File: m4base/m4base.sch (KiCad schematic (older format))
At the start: 38 parts, among them IC1 MCP2562, IC2 STM32F405RxTx, J1 WEST TOP, J2 EAST TOP, P1 SWD_TC, Y1 26M

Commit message: Create top
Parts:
- J?: value CAM -> CAN
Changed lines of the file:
@@
 encoding utf-8
 Sheet 1 1
-Title "M4_TEMPLATE"
+Title "Martlet IV Base"
 Date "2020-02-05"
 Rev "1"
 Comp "CU Spaceflight"
-Comment1 "Drawn By: Sean McGuire"
-Comment2 ""
-Comment3 ""
+Comment1 "Henry Franks"
+Comment2 "Sean McGuire"
+Comment3 "Drawn By:"
 Comment4 ""
 $EndDescr
@@
 P 6700 3250
 F 0 "J?" H 6700 3350 50  0000 C CNN
-F 1 "CAM" H 6700 3050 50  0000 C CNN
+F 1 "CAN" H 6700 3050 50  0000 C CNN
 F 2 "" H 6700 3250 50  0001 C CNN
 F 3 "" H 6700 3250 50  0001 C CNN

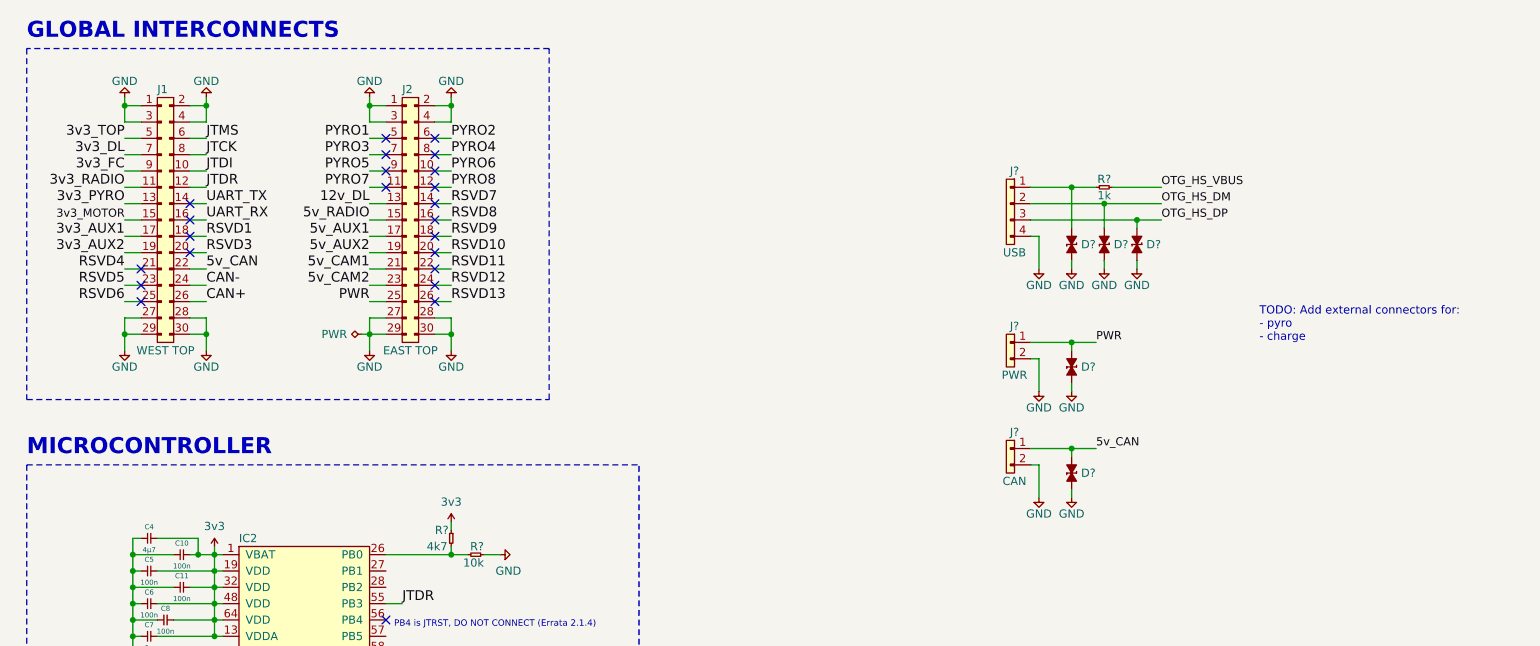
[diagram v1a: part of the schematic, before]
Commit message: Revise global interconnects
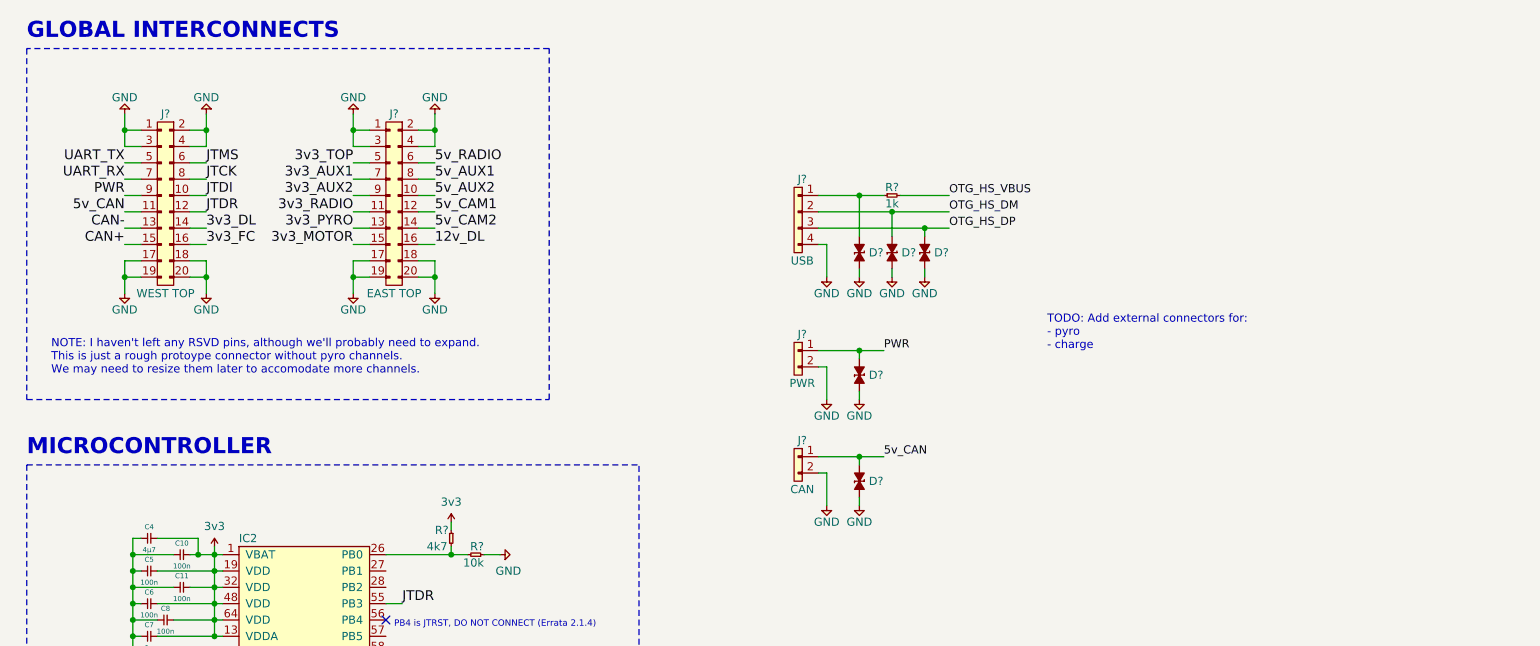
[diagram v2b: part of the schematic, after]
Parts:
- removed J1: WEST TOP, agg:TFML-115-02-L-D-LC, symbol cusf-kicad:CONN_02x15
- removed J2: EAST TOP, agg:TFML-115-02-L-D-LC, symbol cusf-kicad:CONN_02x15
- added J?: WEST TOP, symbol cusf-kicad:CONN_02x10
- added J?: EAST TOP, symbol cusf-kicad:CONN_02x10
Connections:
- net 12v_DL: now also J?.16
- net 3v3_AUX1: now also J?.7
- net 3v3_AUX2: now also J?.9
- net 3v3_DL: now also J?.14
- net 3v3_FC: now also J?.16
- net 3v3_MOTOR: now also J?.15
- net 3v3_PYRO: now also J?.13
- net 3v3_RADIO: now also J?.11
- net 3v3_TOP: now also J?.5
- net 5v_AUX1: now also J?.8
- net 5v_AUX2: now also J?.10
- net 5v_CAM1: now also J?.12
- net 5v_CAM2: now also J?.14
- net 5v_CAN: now also J?.11
- net 5v_RADIO: now also J?.6
- net CAN+: now also J?.15
- net CAN-: now also J?.13
- net GND: now also J?.1, J?.1, J?.17, J?.17, J?.18, J?.18, J?.19, J?.19, J?.2, J?.2, J?.20, J?.20, J?.3, J?.3, J?.4, J?.4
- net JTCK: now also J?.8
- net JTDI: now also J?.10
- net JTDR: now also J?.12
- net JTMS: now also J?.6
- net PWR: now also J?.9
- net UART_RX: now also J?.7
- net UART_TX: now also J?.5
- no-connect marks 24 -> 2
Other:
- note added: "NOTE: I haven't left any RSVD pins, although we'll probably need to expand.\nThis is just a rough protoype connector without pyro channels.\nWe may need to resize them later to accomodate more channels."
- moved on the sheet: D?, J?, R?

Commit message: Cleanup
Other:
- note added: "External Interconnects"
- note added: "NOTE: I haven't left any RSVD pins, although we'll probably need to expand.\nThis is just a rough protoype connector without pyro channels.\nWe may need to resize them later to accomodate more channels.\n-> TODO: Reorganise based on notes from prelim spec"
- note added: "USB Connector"
- note removed: "NOTE: I haven't left any RSVD pins, although we'll probably need to expand.\nThis is just a rough protoype connector without pyro channels.\nWe may need to resize them later to accomodate more channels."
- note removed: "TODO: Add external connectors for:\n- pyro\n- charge"
- moved on the sheet: D?, J?, R?
